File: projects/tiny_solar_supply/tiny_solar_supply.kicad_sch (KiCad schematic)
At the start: 0 parts

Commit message: Start adding symbols
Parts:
- added C1, C2, C3: C, Capacitor_SMD:C_1206_3216Metric_Pad1.33x1.80mm_HandSolder, symbol Device:C
- added D1, D2: SS14, Diode_SMD:D_SMA, symbol Diode:SS14
- added J1, J2, J3, J4: Conn_01x02, symbol Connector_Generic:Conn_01x02
- added L1: L, symbol Device:L
- added Q1: 2N7002, Package_TO_SOT_SMD:SOT-23, symbol Transistor_FET:2N7002
- added R1, R4: 1 MΩ, Resistor_SMD:R_1206_3216Metric_Pad1.30x1.75mm_HandSolder, symbol Device:R
- added R2, R3: R, Resistor_SMD:R_1206_3216Metric_Pad1.30x1.75mm_HandSolder, symbol Device:R

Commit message: Initial commit of schematic
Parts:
- removed J1, J2, J3, J4: Conn_01x02, symbol Connector_Generic:Conn_01x02
- added J1, J2, J3, J4: Conn_01x02, SparkFun-Connector:1x02, symbol SparkFun-Connector:Conn_01x02
- added U1: AP3015AKTR-G1, MH_AP3015A:SOT95P280X145-5N, symbol MH_AP3015A:AP3015AKTR-G1
- C1: value C -> 4.7 µF, 50 V, X7R (0805)
- C2: value C -> 22 µF, 10 V, X7R (1206)
- C3: value C -> 10 pF, 50 V, X7R (0805)
- D1, D2: value SS14 -> SS14 (DO-214AC); footprint Diode_SMD:D_SMA -> SparkFun-Semiconductor-Standard:SMA
- L1: value L -> 10 µH, 680 mA; footprint (none) -> MH_L1:IND_ASPI-0630LR_ABR
- Q1: value 2N7002 -> 2N7002 (SOT-23)
- R1, R4: value 1 MΩ -> 1 MΩ (0805, 0.125 W)
- R2: value R -> 604 kΩ, 1% (0805, 0.125 W)
- R3: value R -> 10 kΩ (0805, 0.125 W)
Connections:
- net GND: now reaches R4.1
- net GND: now also C1.1, C2.1, Q1.2 (S), R2.1, J1.2 (Pin_2), J2.2 (Pin_2), J4.2 (Pin_2), U1.2 (GND)
- net at R4.2: now also D2.2 (A), Q1.1 (G), J4.1 (Pin_1)
- net at L1.1: now also C1.2, R3.2, J3.2 (Pin_2), U1.5 (VIN)
- net at L1.2: now also D1.2 (A), U1.1 (SW)
- net at C2.2: now also C3.2, D1.1 (K), R1.2, J1.1 (Pin_1)
- net at R3.1: now also Q1.3 (D), U1.4 (~{SHDN})
- net at R1.1: now also C3.1, R2.2, U1.3 (FB)
- net at D2.1 (K): now also J2.1 (Pin_1), J3.1 (Pin_1)
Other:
- note added: "Battery"
- note added: "ON / OFF"
- note added: "Solar Panel"
- moved on the sheet: C1, C2, C3, D1, D2, L1, Q1, R1, R2, R3, R4

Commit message: Schematic - complete with ERC
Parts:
- J1: MH_Role (none) -> Output
- J2: MH_Role (none) -> Battery
- J3: MH_Role (none) -> ON/OFF switch
- J4: MH_Role (none) -> Solar Panel
- renumbered Q1 to T1
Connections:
- net SOLAR_POSITIVE: now reaches D2.2 (A), J4.1 (Pin_1), R4.2, T1.1 (G)
- net OUTPUT_POSITIVE: now reaches C2.2, C3.2, D1.1 (K), J1.1 (Pin_1), R1.2
- net BATT_POSITIVE: now reaches D2.1 (K), J2.1 (Pin_1), J3.1 (Pin_1)
- net GND renamed GNDD
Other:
- note removed: "Battery"
- note removed: "ON / OFF"
- note removed: "Solar Panel"
- moved on the sheet: C1, C2, C3, D1, D2, J1, J2, J3, J4, L1, R1, R2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

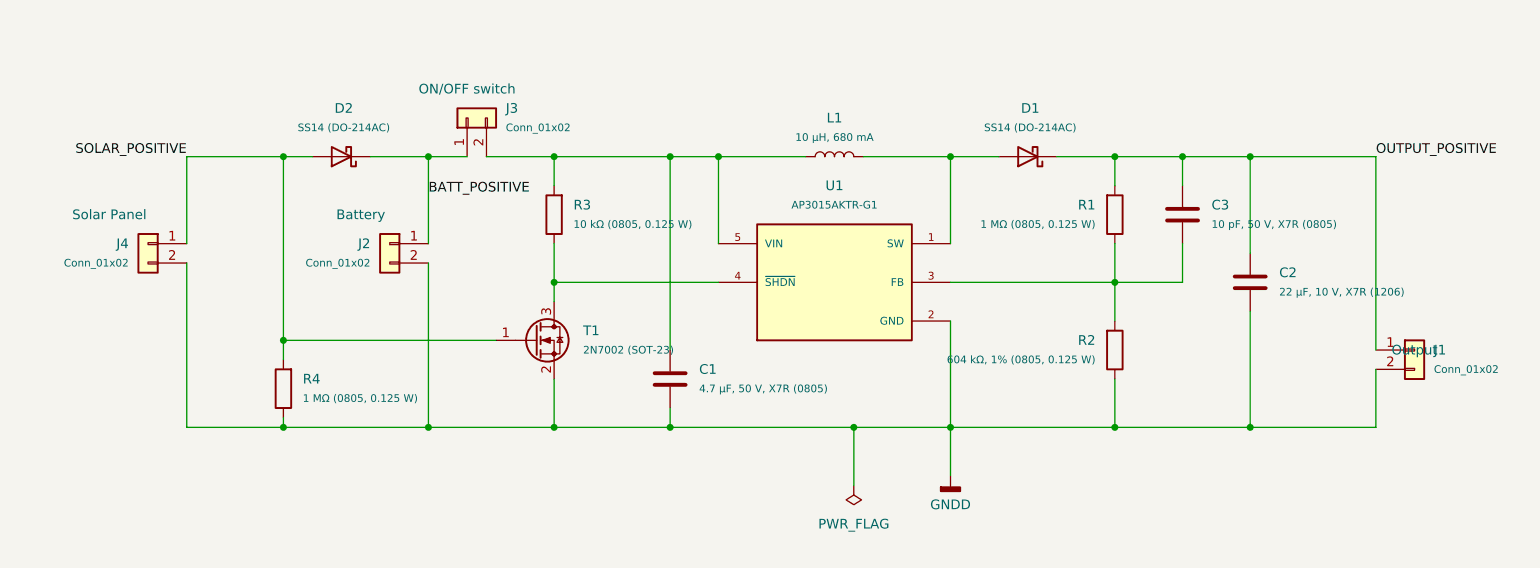
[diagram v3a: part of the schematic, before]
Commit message: Create v1.0 - first version sent for manufacturing
- in folder versions/ save versions v0.1 and v1.0
- in folder gerbers/ export gerbers of version v1.0
- in folder assets/ rename figures of v0.1 and create figures of v1.0
- update file README.md
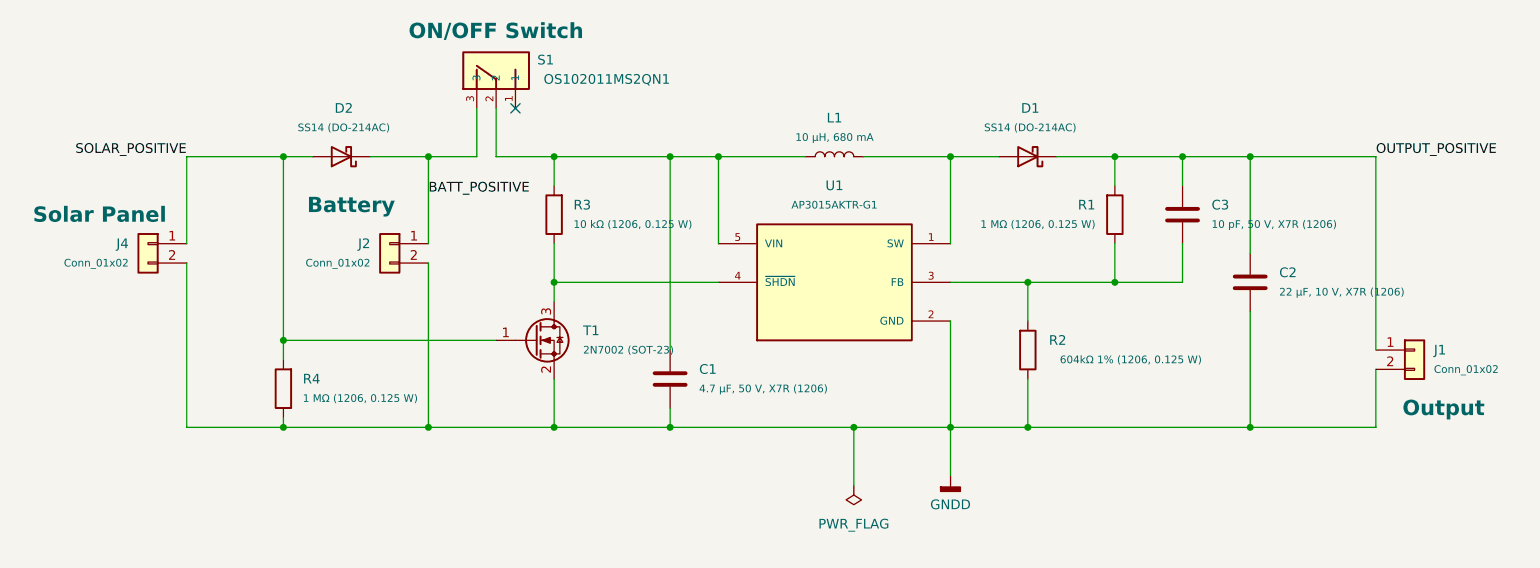
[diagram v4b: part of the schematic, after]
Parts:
- removed J3: Conn_01x02, SparkFun-Connector:1x02, symbol SparkFun-Connector:Conn_01x02
- added S1: OS102011MS2QN1, MH_Slide_Switch:SW_OS102011MS2QN1, symbol MH_Switch:OS102011MS2QN1
- C1: value 4.7 µF, 50 V, X7R (0805) -> 4.7 µF, 50 V, X7R (1206)
- C3: value 10 pF, 50 V, X7R (0805) -> 10 pF, 50 V, X7R (1206)
- R1, R4: value 1 MΩ (0805, 0.125 W) -> 1 MΩ (1206, 0.125 W)
- R2: value 604 kΩ, 1% (0805, 0.125 W) -> 604kΩ 1% (1206, 0.125 W)
- R3: value 10 kΩ (0805, 0.125 W) -> 10 kΩ (1206, 0.125 W)
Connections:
- net BATT_POSITIVE: now also S1.3
- net at C1.2, L1.1, R3.2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: now also S1.2
- no-connect marks 0 -> 1
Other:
- moved on the sheet: R2

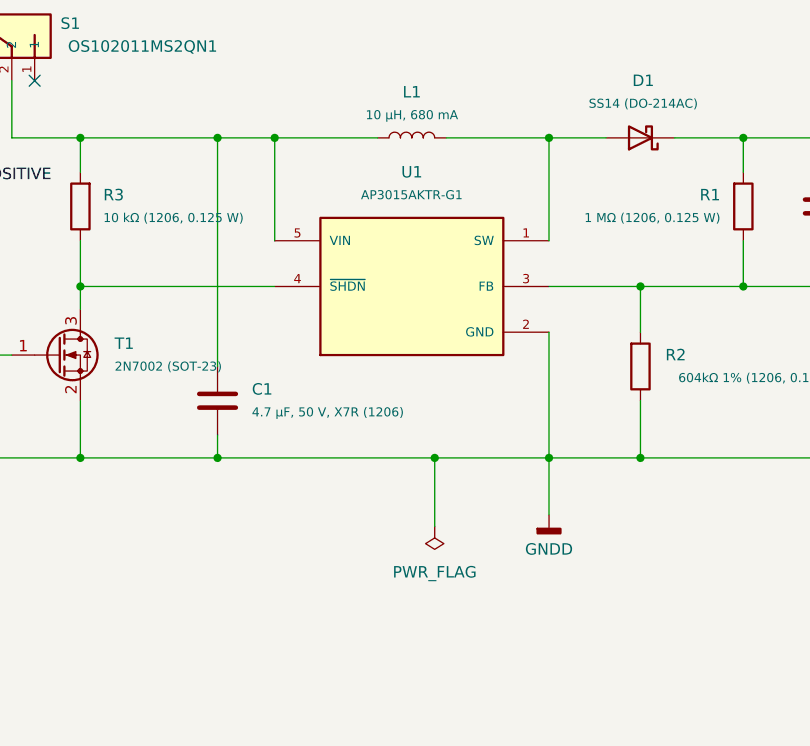
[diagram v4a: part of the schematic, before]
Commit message: tiny_solar_supply v1.1 initial commit
- improve silkscreen: whit bkg on user labels
- improve routing: vias to GND plane
- add datasheets of AP3015 and L1
- fix switch ON/OFF labels (were reversed)

Pending: Fix wrong L1 footprint.
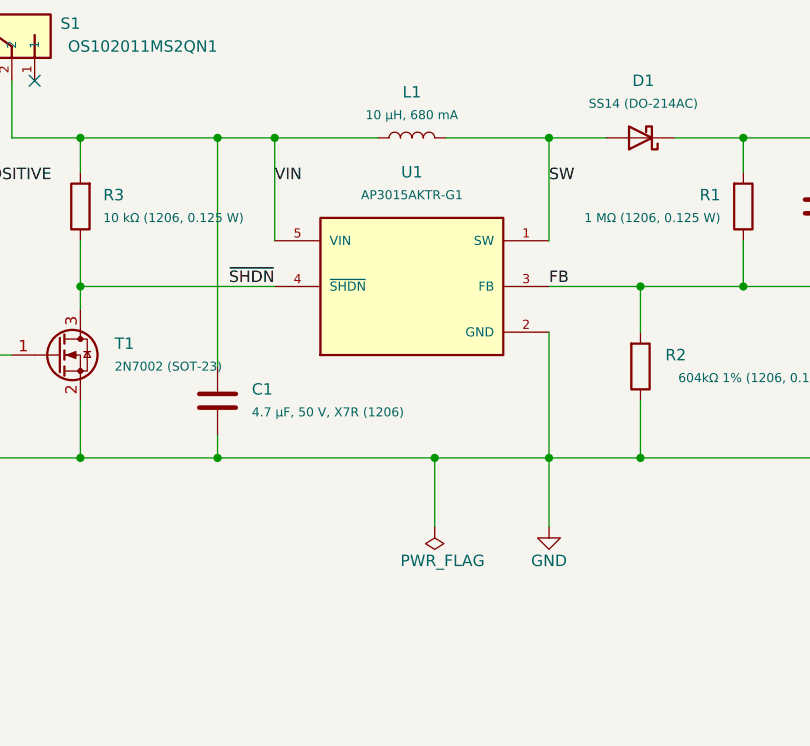
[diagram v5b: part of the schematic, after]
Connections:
- net SW: now reaches D1.2 (A), L1.2, U1.1 (SW)
- net FB: now reaches C3.1, R1.1, R2.2, U1.3 (FB)
- net ~{SHDN}: now reaches R3.1, T1.3 (D), U1.4 (~{SHDN})
- net VIN: now reaches C1.2, L1.1, R3.2, S1.2, U1.5 (VIN)
- net GNDD renamed GND
